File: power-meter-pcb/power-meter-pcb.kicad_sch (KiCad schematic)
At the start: 22 parts, among them J1 Crank interconnect, J2 Debug, SW1 EN, SW2 BOOT, U2 P3T1755, U8 ESP32-S3-MINI-1

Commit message: Re-centred schematics, added header for spare GPIO pins, touched up logos
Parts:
- added J7: Spare GPIO pins, Connector_PinHeader_2.00mm:PinHeader_1x05_P2.00mm_Vertical, symbol Connector:Conn_01x05_Pin
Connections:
- net Battery voltage: now reaches U8.16 (IO12)
- net GPIO.15: now reaches U8.19 (IO15)
- net GPIO.15: now also J7.5 (Pin_5)
- net GPIO.17: now reaches U8.21 (IO17)
- net GPIO.17: now also J7.4 (Pin_4)
- net GPIO.18: now reaches U8.22 (IO18)
- net GPIO.18: now also J7.3 (Pin_3)
- net GPIO.33: now reaches U8.28 (IO33)
- net GPIO.33: now also J7.1 (Pin_1)
- net USB and power supply/Battery voltage renamed GPIO.26
- net GPIO.26: now also J7.2 (Pin_2)
- no-connect marks 19 -> 14

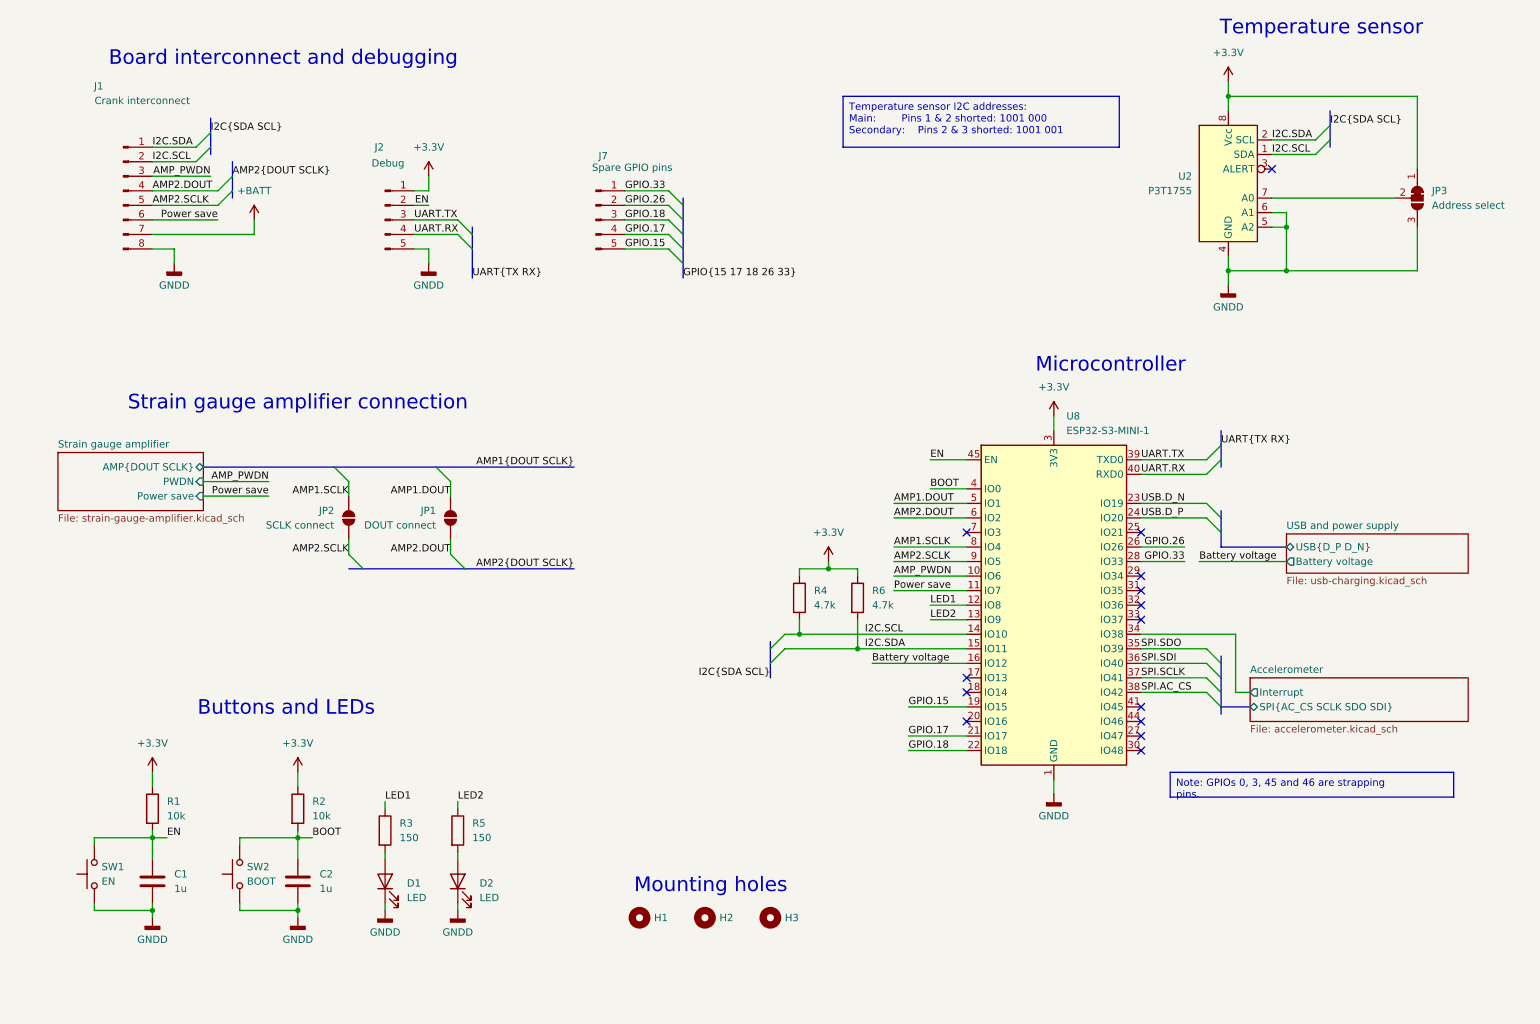
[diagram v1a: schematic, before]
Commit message: Added LED driven by temp sensor, updated numbering
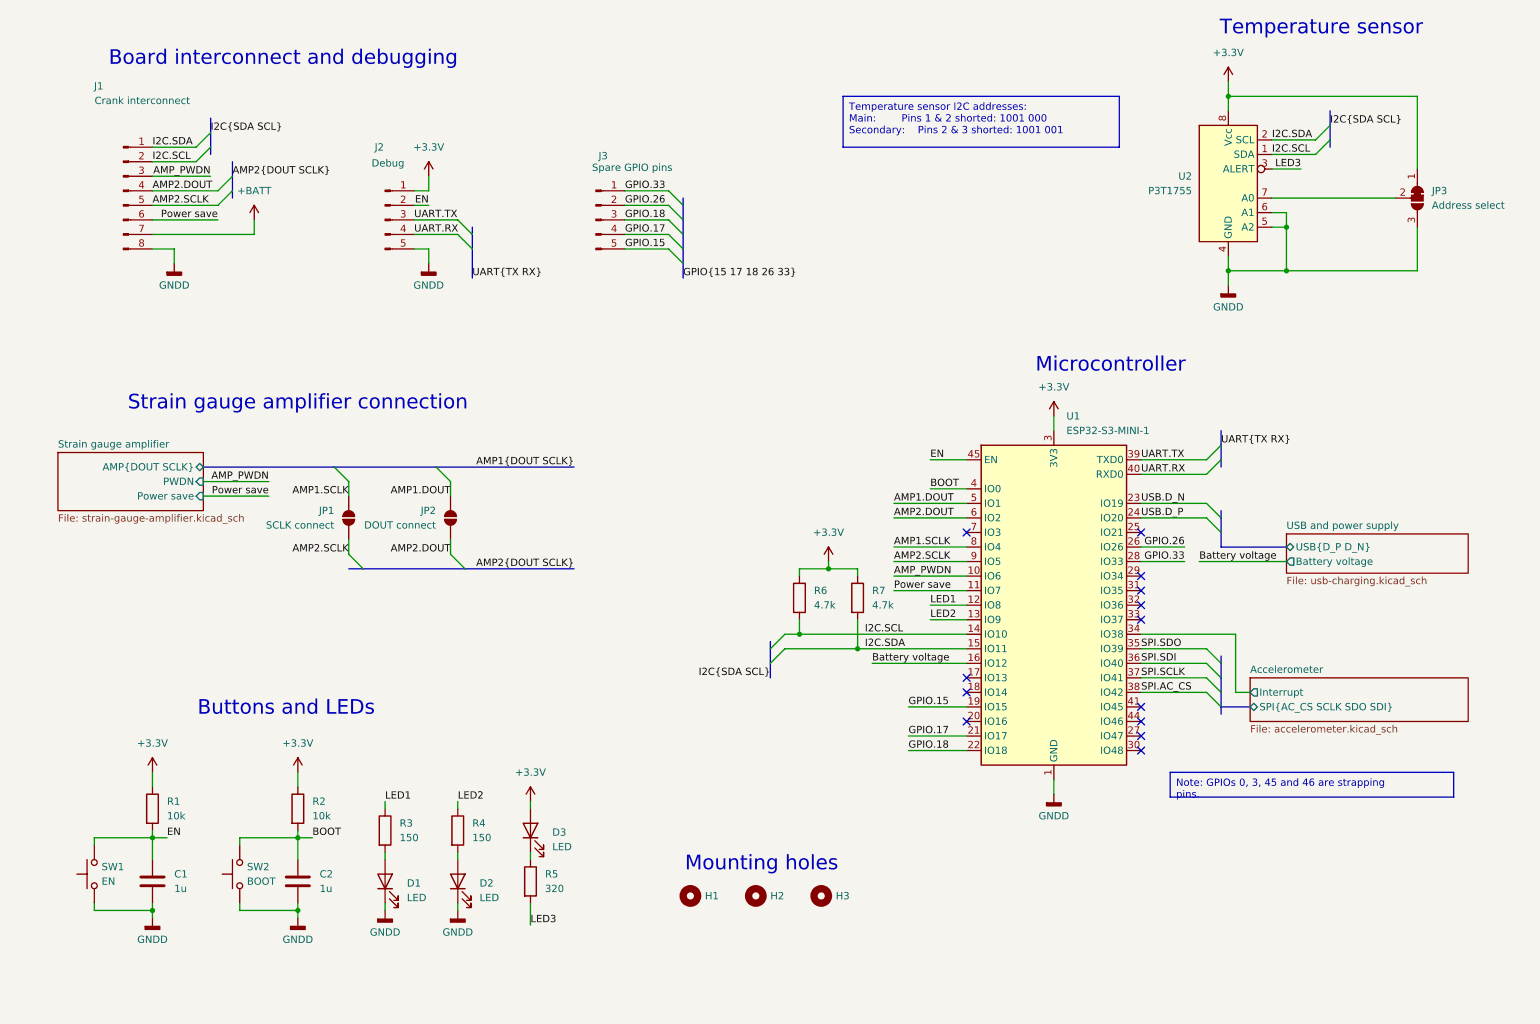
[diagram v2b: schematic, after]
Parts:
- added D3: LED, LED_SMD:LED_0603_1608Metric_Pad1.05x0.95mm_HandSolder, symbol Device:LED
- added R5: 320, Resistor_SMD:R_0603_1608Metric_Pad0.98x0.95mm_HandSolder, symbol Device:R
- J3: renamed from J7; PlaceOnSecondary (none) -> No
- U1: renamed from U8; PlaceOnSecondary (none) -> No
- renumbered JP2 to JP1, JP1 to JP2, R5 to R4, R4 to R6, R6 to R7
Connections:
- net +3.3V: now also D3.2 (A)
- net LED3: now reaches U2.3 (ALERT)
- net LED3: now also R5.2
- new net: D3.1 (K), R5.1
- no-connect marks 14 -> 13
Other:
- moved on the sheet: H1, H2, H3

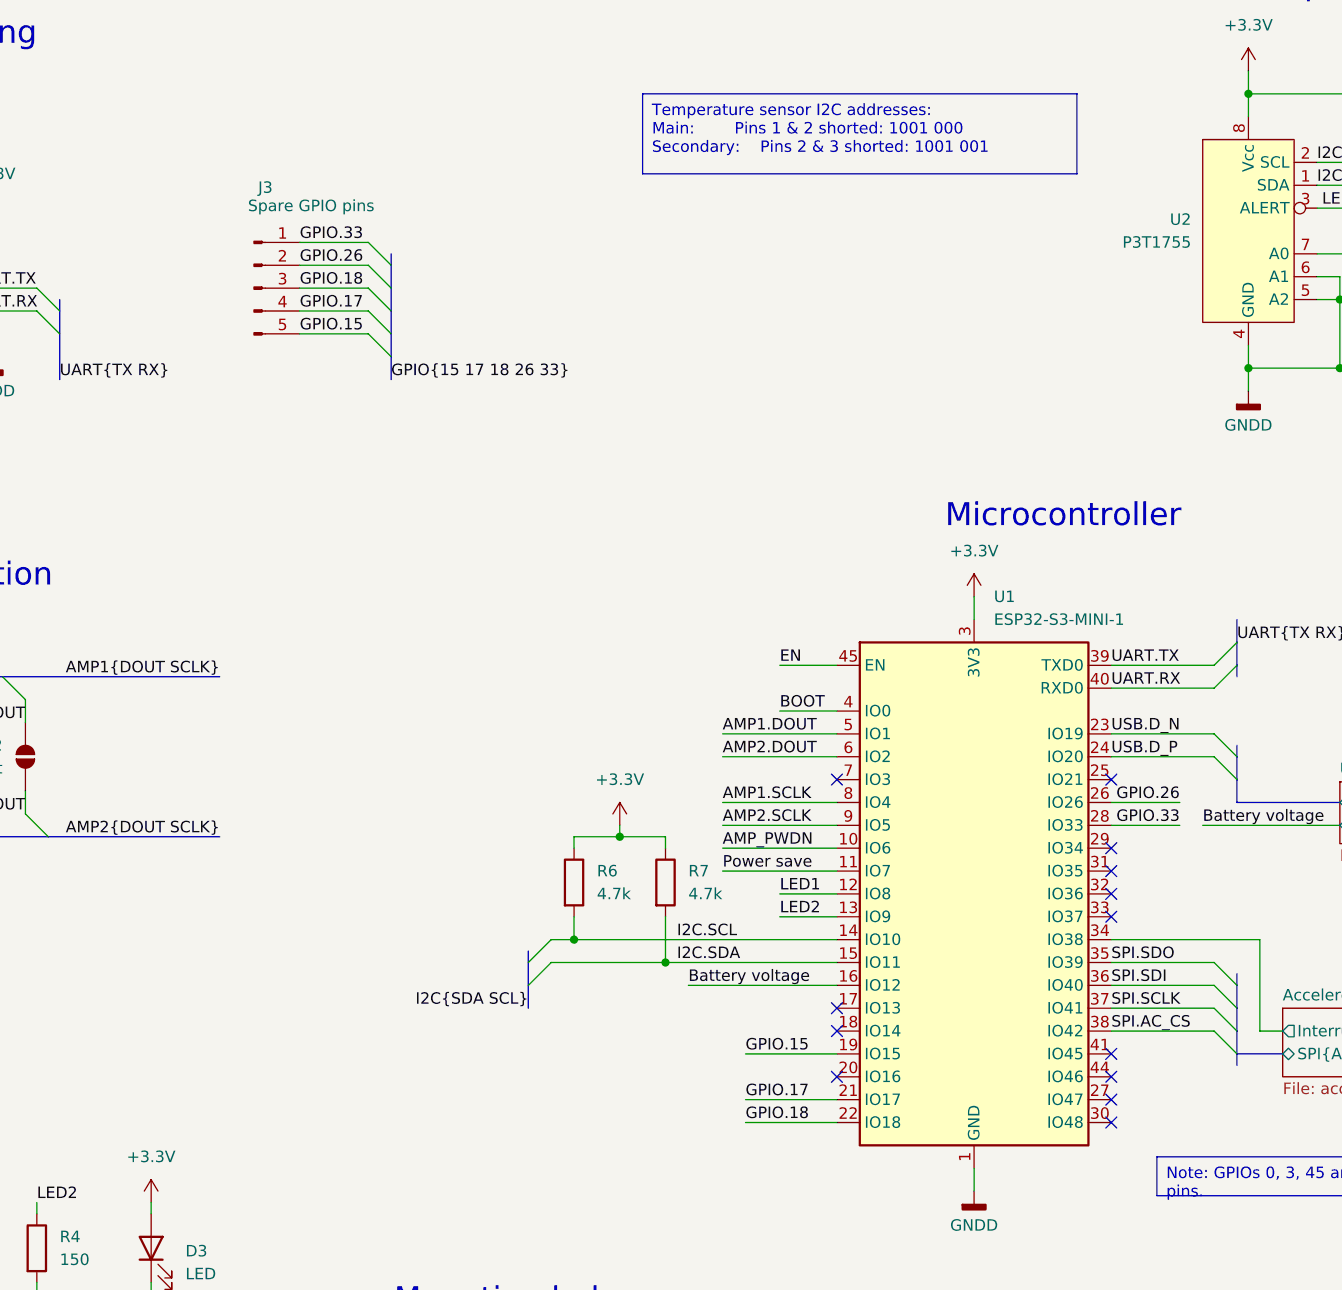
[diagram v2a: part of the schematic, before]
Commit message: Cap on ADC DC pin moved to next to pin
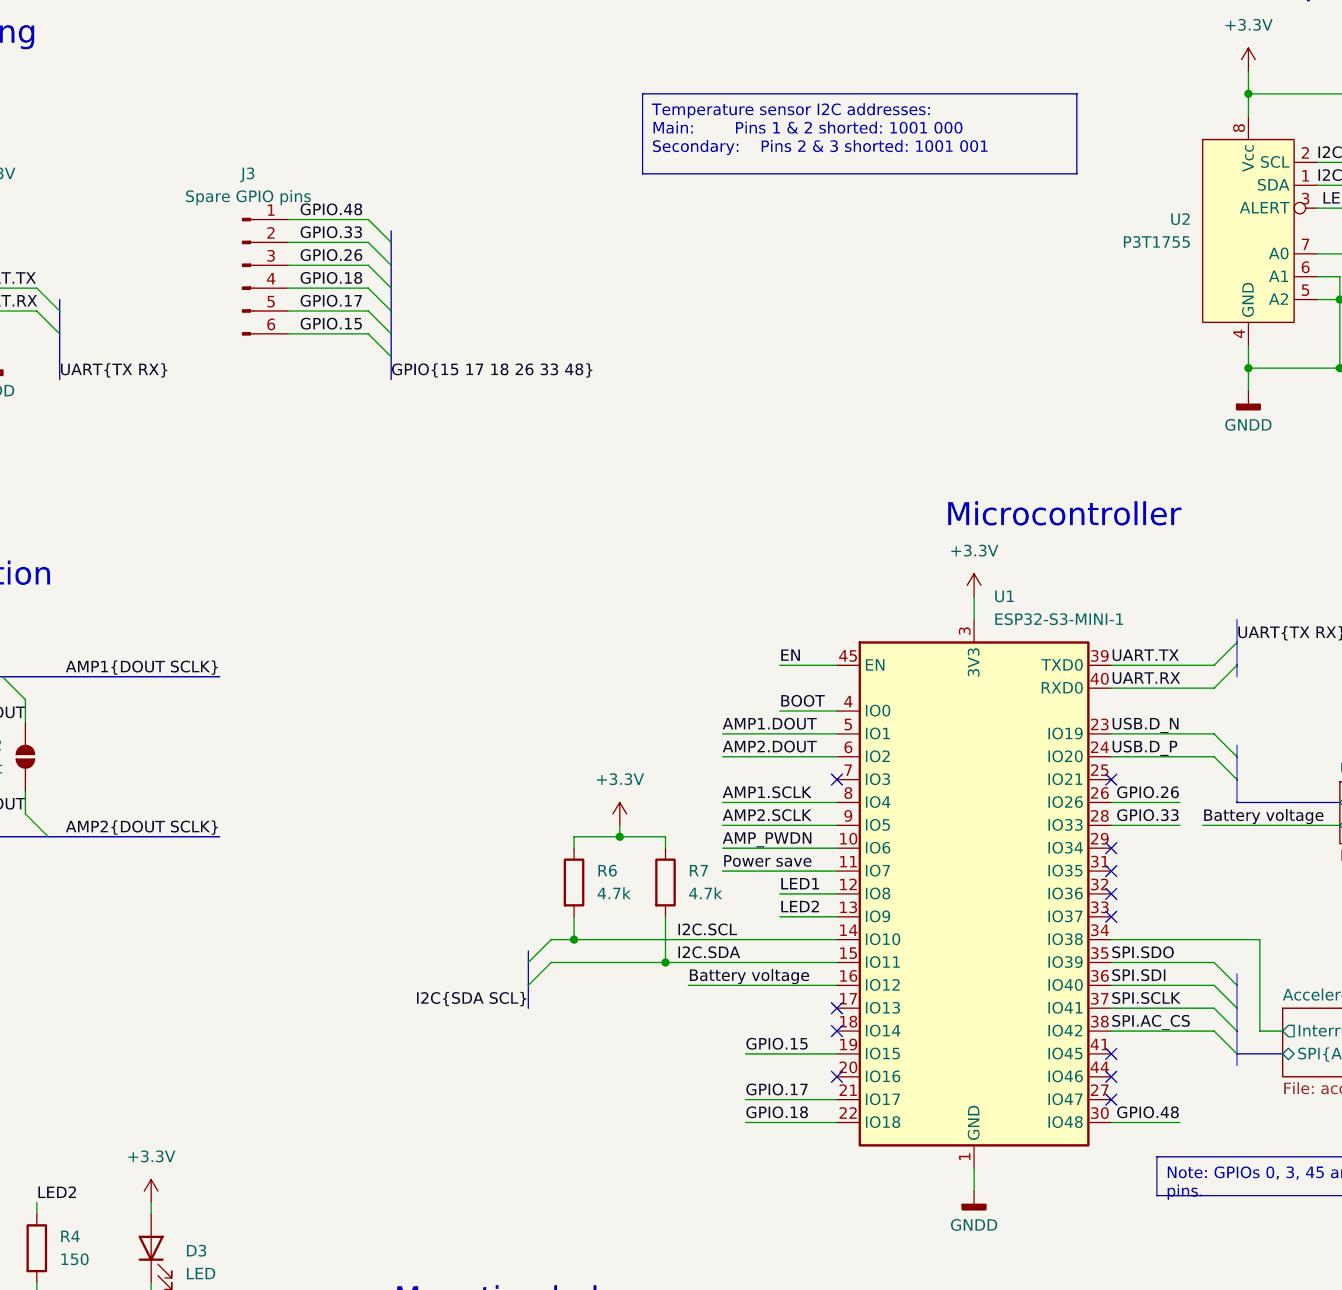
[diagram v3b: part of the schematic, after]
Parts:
- removed J3: Spare GPIO pins, Connector_PinHeader_2.00mm:PinHeader_1x05_P2.00mm_Vertical, symbol Connector:Conn_01x05_Pin
- added J3: Spare GPIO pins, Connector_PinHeader_2.00mm:PinHeader_1x06_P2.00mm_Vertical, symbol Connector:Conn_01x06_Pin
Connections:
- net GPIO.15: now also J3.6 (Pin_6)
- net GPIO.17: now also J3.5 (Pin_5)
- net GPIO.18: now also J3.4 (Pin_4)
- net GPIO.26: now also J3.3 (Pin_3)
- net GPIO.33: now also J3.2 (Pin_2)
- net GPIO.48: now reaches U1.30 (IO48)
- net GPIO.48: now also J3.1 (Pin_1)
- no-connect marks 13 -> 12
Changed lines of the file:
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@@
 	(title_block
 		(title "Cycling power meter FYP")
-		(date "2024-07-11")
-		(rev "V1.0.3")
+		(date "2024-07-15")
+		(rev "V1.0.4")
 		(company "Monash Human Power - Jotham Gates & Oscar Varney")
 		(comment 1 "For the secondary crank, set J3 to short pins 2 and 3 and short J1 and J2.")
@@
 	)
 	(no_connect
-		(at 214.63 148.59)
-	)
-	(no_connect
 		(at 184.15 135.89)
 	)
@@
 	)
 	(bus_entry
+		(at 132.08 48.26)
+		(size 2.54 2.54)
+		(stroke
+			(width 0)
+			(type default)
+		)
+	)
+	(bus_entry
 		(at 95.25 58.42)
 		(size 2.54 2.54)
@@
 	(wire
 		(pts
-			(xy 124.46 53.34) (xy 132.08 53.34)
+			(xy 123.19 53.34) (xy 132.08 53.34)
 		)
 		(stroke
@@
 	(wire
 		(pts
-			(xy 124.46 60.96) (xy 132.08 60.96)
+			(xy 123.19 60.96) (xy 132.08 60.96)
 		)
 		(stroke
@@
 	(wire
 		(pts
+			(xy 214.63 148.59) (xy 222.25 148.59)
+		)
+		(stroke
+			(width 0)
+			(type default)
+		)
+	)
+	(wire
+		(pts
 			(xy 152.4 128.27) (xy 154.94 128.27)
 		)
@@
 		)
 	)
+	(bus
+		(pts
+			(xy 134.62 50.8) (xy 134.62 53.34)
+		)
+		(stroke
+			(width 0)
+			(type default)
+		)
+	)
 	(wire
 		(pts
-			(xy 124.46 58.42) (xy 132.08 58.42)
+			(xy 123.19 58.42) (xy 132.08 58.42)
 		)
 		(stroke
@@
 		)
 	)
+	(bus
+		(pts
+			(xy 134.62 49.53) (xy 134.62 50.8)
+		)
+		(stroke
+			(width 0)
+			(type default)
+		)
+	)
 	(wire
 		(pts
@@
 	(wire
 		(pts
-			(xy 124.46 50.8) (xy 132.08 50.8)
+			(xy 123.19 50.8) (xy 132.08 50.8)
 		)
 		(stroke
@@
 		)
 	)
-	(bus
-		(pts
-			(xy 134.62 52.07) (xy 134.62 53.34)
-		)
-		(stroke
-			(width 0)
-			(type default)
-		)
-	)
 	(wire
 		(pts
@@
 	(wire
 		(pts
-			(xy 124.46 55.88) (xy 132.08 55.88)
+			(xy 123.19 55.88) (xy 132.08 55.88)
 		)
 		(stroke
@@
 	(wire
 		(pts
+			(xy 123.19 48.26) (xy 132.08 48.26)
+		)
+		(stroke
+			(width 0)
+			(type default)
+		)
+	)
+	(wire
+		(pts
 			(xy 224.79 115.57) (xy 240.03 115.57)
 		)
@@
 		)
 	)
-	(label "GPIO{15 17 18 26 33}"
+	(label "GPIO{15 17 18 26 33 48}"
 		(at 134.62 66.04 0)
 		(fields_autoplaced yes)
@@
 		)
 	)
+	(label "GPIO.48"
+		(at 222.25 148.59 180)
+		(fields_autoplaced yes)
+		(effects
+			(font
+				(size 1.27 1.27)
+			)
+			(justify right bottom)
+		)
+	)
 	(label "AMP2.SCLK"
 		(at 41.91 53.34 0)
@@
 		)
 	)
+	(label "GPIO.48"
+		(at 124.46 48.26 0)
+		(fields_autoplaced yes)
+		(effects
+			(font
+				(size 1.27 1.27)
+			)
+			(justify left bottom)
+		)
+	)
 	(label "SPI.SDI"
 		(at 214.63 133.35 0)
@@
 	)
 	(symbol
-		(lib_id "Connector:Conn_01x05_Pin")
-		(at 119.38 55.88 0)
-		(unit 1)
-		(exclude_from_sim no)
-		(in_bom yes)
-		(on_board yes)
-		(dnp no)
-		(property "Reference" "J3"
-			(at 120.65 44.704 0)
-			(effects
-				(font
-					(size 1.27 1.27)
-				)
-			)
-		)
-		(property "Value" "Spare GPIO pins"
-			(at 125.73 46.736 0)
-			(effects
-				(font
-					(size 1.27 1.27)
-				)
-			)
-		)
-		(property "Footprint" "Connector_PinHeader_2.00mm:PinHeader_1x05_P2.00mm_Vertical"
-			(at 119.38 55.88 0)
-			(effects
-				(font
-					(size 1.27 1.27)
-				)
-				(hide yes)
-			)
-		)
-		(property "Datasheet" "~"
-			(at 119.38 55.88 0)
-			(effects
-				(font
-					(size 1.27 1.27)
-				)
-				(hide yes)
-			)
-		)
-		(property "Description" "Generic connector, single row, 01x05, script generated"
-			(at 119.38 55.88 0)
-			(effects
-				(font
-					(size 1.27 1.27)
-				)
-				(hide yes)
-			)
-		)
-		(property "PlaceOnSecondary" "No"
-			(at 119.38 55.88 0)
-			(effects
-				(font
-					(size 1.27 1.27)
-				)
-				(hide yes)
-			)
-		)
-		(property "Sim.Device" ""
-			(at 119.38 55.88 0)
-			(effects
-				(font
-					(size 1.27 1.27)
-				)
-				(hide yes)
-			)
-		)
-		(property "Sim.Pins" ""
-			(at 119.38 55.88 0)
-			(effects
-				(font
-					(size 1.27 1.27)
-				)
-				(hide yes)
-			)
-		)
-		(pin "3"
-		)
-		(pin "4"
-		)
-		(pin "2"
-		)
-		(pin "5"
-		)
-		(pin "1"
-		)
-		(instances
-			(project ""
-				(path "/73d1dc3f-3725-4767-8c11-2d32e15ee0d6"
-					(reference "J3")
-					(unit 1)
-				)
-			)
-		)
-	)
-	(symbol
 		(lib_id "power:GNDD")
 		(at 90.17 63.5 0)
@@
 					(unit 1)
 				)
+			)
+		)
+	)
+	(symbol
+		(lib_id "Connector:Conn_01x06_Pin")
+		(at 118.11 53.34 0)
+		(unit 1)
+		(exclude_from_sim no)
+		(in_bom yes)
+		(on_board yes)
+		(dnp no)
+		(fields_autoplaced yes)
+		(property "Reference" "J3"
+			(at 118.745 43.18 0)
+			(effects
+				(font
+					(size 1.27 1.27)
+				)
+			)
+		)
+		(property "Value" "Spare GPIO pins"
+			(at 118.745 45.72 0)
+			(effects
+				(font
+					(size 1.27 1.27)
+				)
+			)
+		)
+		(property "Footprint" "Connector_PinHeader_2.00mm:PinHeader_1x06_P2.00mm_Vertical"
+			(at 118.11 53.34 0)
+			(effects
+				(font
+					(size 1.27 1.27)
+				)
+				(hide yes)
+			)
+		)
+		(property "Datasheet" "~"
+			(at 118.11 53.34 0)
+			(effects
+				(font
+					(size 1.27 1.27)
+				)
+				(hide yes)
+			)
+		)
+		(property "Description" "Generic connector, single row, 01x06, script generated"
+			(at 118.11 53.34 0)
+			(effects
+				(font
+					(size 1.27 1.27)
+				)
+				(hide yes)
+			)
+		)
+		(pin "2"
+		)
+		(pin "3"
+		)
+		(pin "1"
+		)
+		(pin "5"
+		)
+		(pin "6"
+		)
+		(pin "4"
+		)
+		(instances
+			(project ""
+				(path "/73d1dc3f-3725-4767-8c11-2d32e15ee0d6"
+					(reference "J3")
+					(unit 1)
+				)
